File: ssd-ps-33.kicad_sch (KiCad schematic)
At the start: 0 parts

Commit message: Put controller and filter capacitors to schematic
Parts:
- added C1, C2: 10uF, Capacitor_SMD:C_0805_2012Metric, symbol Device:C
- added C3: 0.1uF, Capacitor_SMD:C_0603_1608Metric_Pad1.08x0.95mm_HandSolder, symbol Device:C
- added C4, C5, C6: 22uF, Capacitor_SMD:C_0805_2012Metric, symbol Device:C
- added L1: 2.2µH, symbol Device:L_Ferrite
- added U1: TPS563252, Package_TO_SOT_SMD:SOT-563, symbol ssd-ps-33:TPS56325x
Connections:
- new net GND: U1.3 (GND)

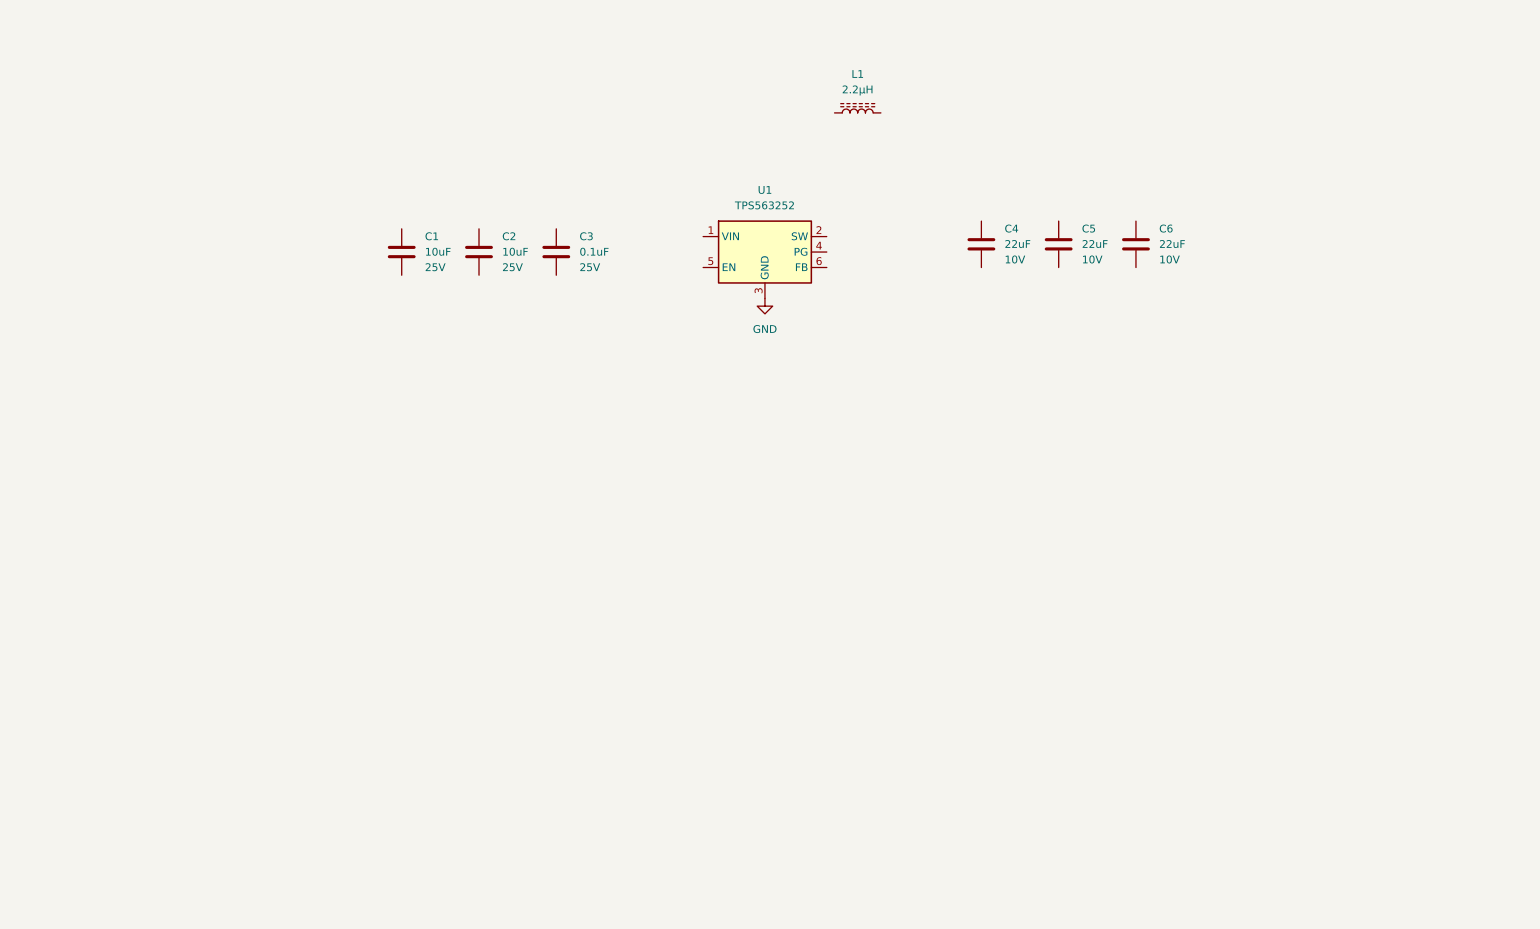
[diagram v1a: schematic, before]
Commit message: Create main schematics without connectors for now
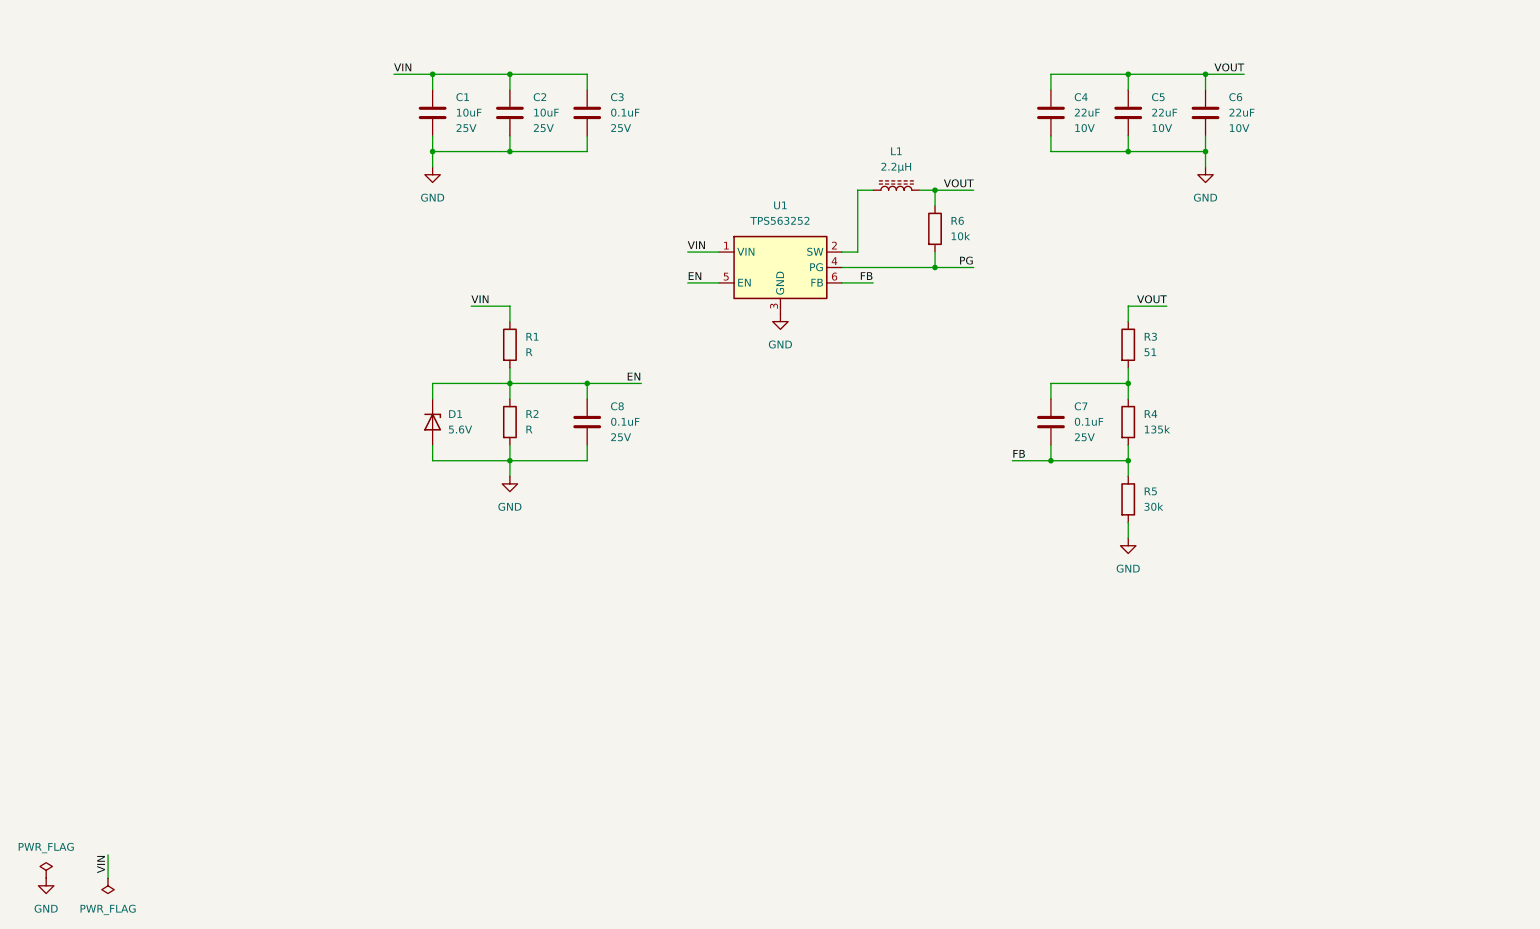
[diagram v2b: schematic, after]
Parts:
- added C7, C8: 0.1uF, Capacitor_SMD:C_0603_1608Metric_Pad1.08x0.95mm_HandSolder, symbol Device:C
- added D1: 5.6V, Diode_SMD:D_SOD-323_HandSoldering, symbol Device:D_Zener
- added R1, R2: R, Resistor_SMD:R_0603_1608Metric_Pad0.98x0.95mm_HandSolder, symbol Device:R
- added R3: 51, Resistor_SMD:R_0603_1608Metric_Pad0.98x0.95mm_HandSolder, symbol Device:R
- added R4: 135k, Resistor_SMD:R_0603_1608Metric_Pad0.98x0.95mm_HandSolder, symbol Device:R
- added R5: 30k, Resistor_SMD:R_0603_1608Metric_Pad0.98x0.95mm_HandSolder, symbol Device:R
- added R6: 10k, Resistor_SMD:R_0603_1608Metric_Pad0.98x0.95mm_HandSolder, symbol Device:R
- L1: footprint (none) -> Inductor_SMD:L_Chilisin_BWVS00505040
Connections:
- net GND: now also C1.2, C2.2, C3.2, C4.2, C5.2, C6.2, C8.2, D1.2 (A), R2.2, R5.2
- net VOUT: now reaches C4.1
- net VOUT: now also C5.1, C6.1, L1.2, R3.1, R6.1
- net at L1.1: now also U1.2 (SW)
- net VIN: now reaches U1.1 (VIN)
- net VIN: now also C1.1, C2.1, C3.1, R1.1
- net PG: now reaches U1.4 (PG)
- net PG: now also R6.2
- net EN: now reaches U1.5 (EN)
- net EN: now also C8.1, D1.1 (K), R1.2, R2.1
- net FB: now reaches U1.6 (FB)
- net FB: now also C7.2, R4.2, R5.1
- new net: C7.1, R3.2, R4.1
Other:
- moved on the sheet: C1, C2, C3, C4, C5, C6, L1, U1

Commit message: Draft routing, board size and select connectors
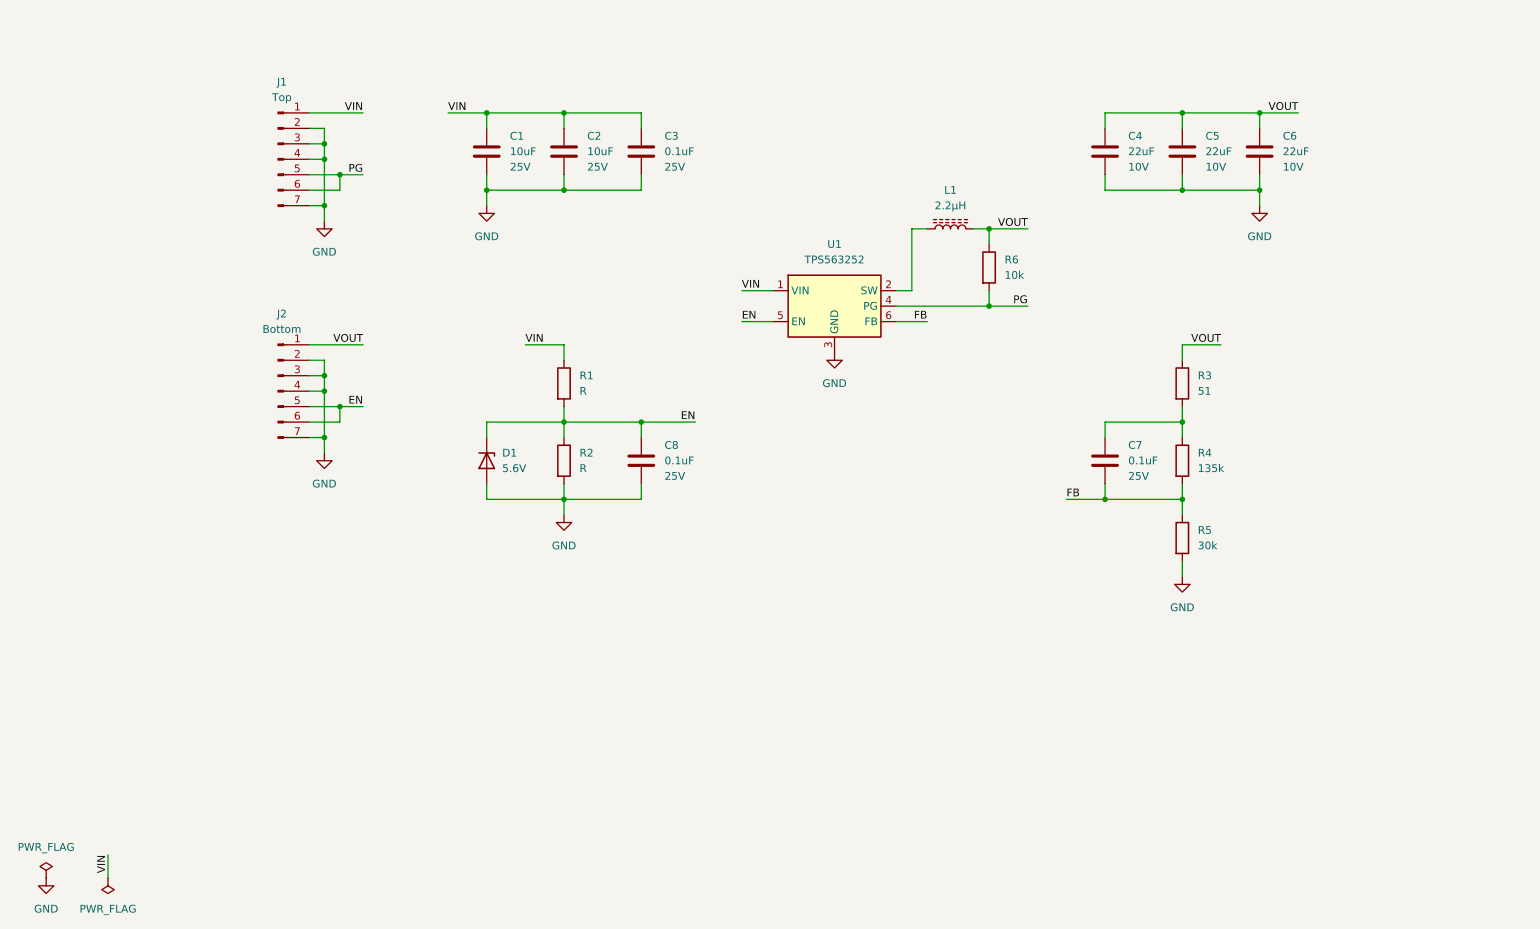
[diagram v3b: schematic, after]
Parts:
- added J1: Top, ssd-ps-33:PinHeader_1x07_P2.54mm_Vertical_No_Silkscreen, symbol Connector:Conn_01x07_Pin
- added J2: Bottom, ssd-ps-33:PinHeader_1x07_P2.54mm_Vertical_No_Silkscreen, symbol Connector:Conn_01x07_Pin
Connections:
- net EN: now also J2.5 (Pin_5), J2.6 (Pin_6)
- net GND: now also J1.2 (Pin_2), J1.3 (Pin_3), J1.4 (Pin_4), J1.7 (Pin_7), J2.2 (Pin_2), J2.3 (Pin_3), J2.4 (Pin_4), J2.7 (Pin_7)
- net PG: now also J1.5 (Pin_5), J1.6 (Pin_6)
- net VIN: now also J1.1 (Pin_1)
- net VOUT: now also J2.1 (Pin_1)
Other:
- moved on the sheet: C1, C2, C3, C4, C5, C6, C7, C8, D1, L1, R1, R2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

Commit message: Set values for enable network and fix DRC errors
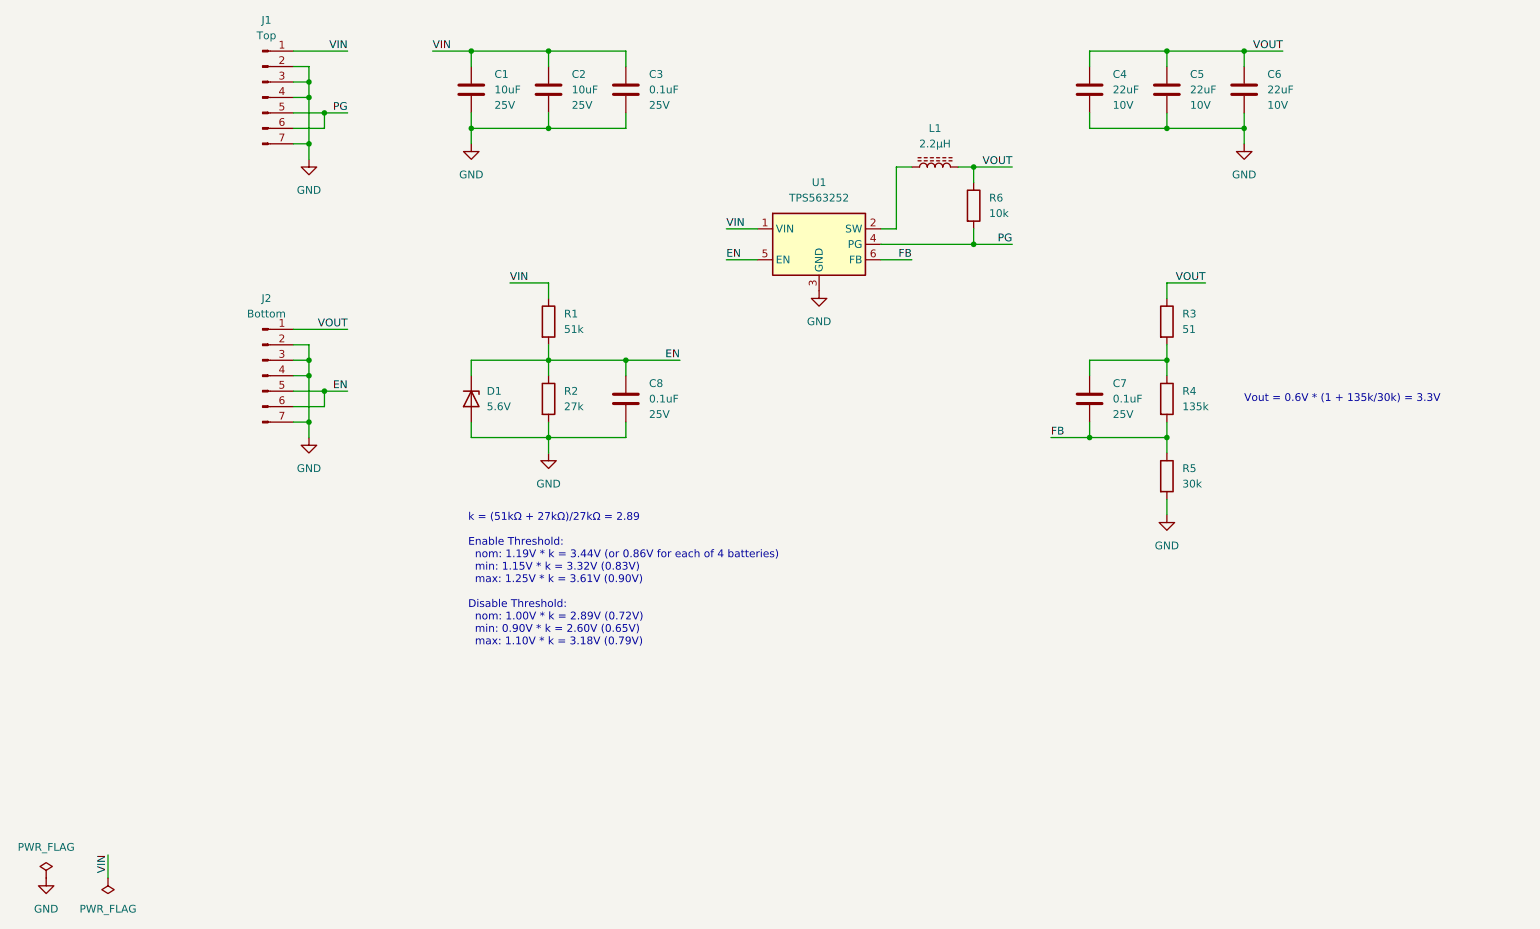
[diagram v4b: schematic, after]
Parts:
- R1: value R -> 51k
- R2: value R -> 27k
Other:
- note added: "Vout = 0.6V * (1 + 135k/30k) = 3.3V"
- note added: "k = (51kΩ + 27kΩ)/27kΩ = 2.89 Enable Threshold: nom: 1.19V * k = 3.44V (or 0.86V for each of 4 batteries) min: 1.15V * k = 3.32V (0.83V) max: 1.25V * k = 3.61V (0.90V) Disable Threshold: nom: 1.00V * k = 2.89V (0.72V) min: 0.90V * k = 2.60V (0.65V) max: 1.10V * k = 3.18V (0.79V)"
- moved on the sheet: C1, C2, C3, C4, C5, C6, C7, C8, D1, J1, J2, L1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

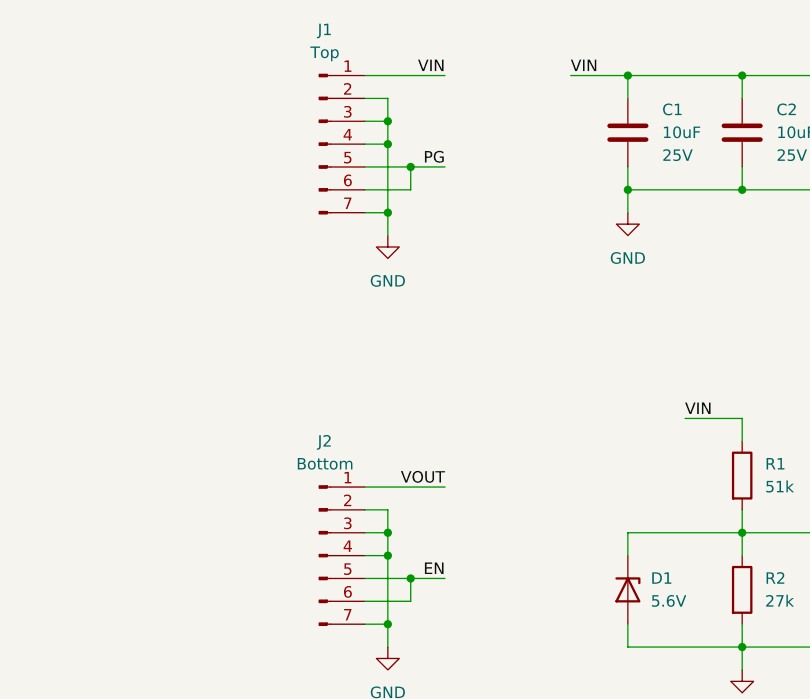
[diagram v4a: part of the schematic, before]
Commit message: Add designators to pins and board name
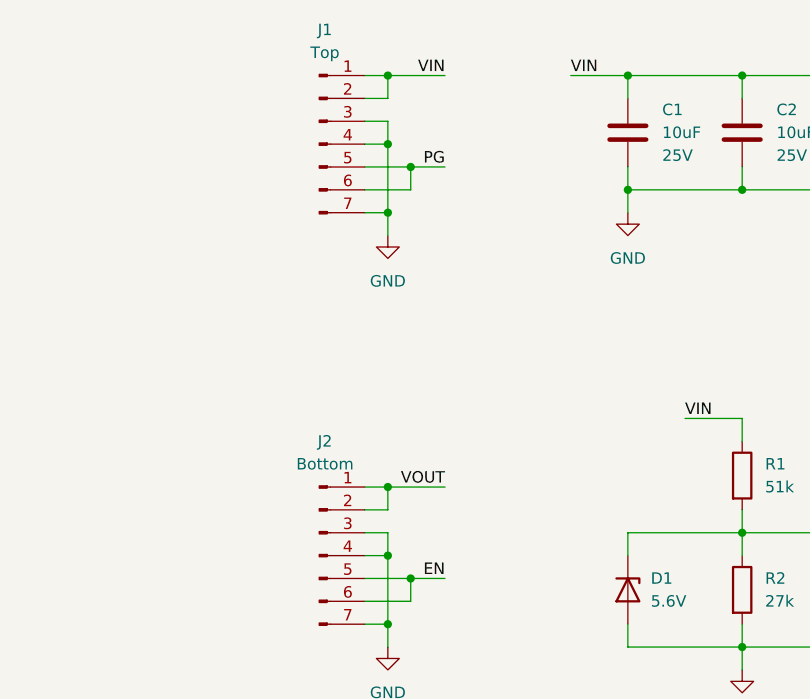
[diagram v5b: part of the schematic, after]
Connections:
- net GND: no longer J1.2 (Pin_2), J2.2 (Pin_2)
- net VIN: now also J1.2 (Pin_2)
- net VOUT: now also J2.2 (Pin_2)
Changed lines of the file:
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@@
+	)
+	(junction
+		(at 62.23 59.69)
+		(diameter 0)
+		(color 0 0 0 0)
 	)
 	(junction
@@
 	)
 	(junction
-		(at 62.23 110.49)
-		(diameter 0)
-		(color 0 0 0 0)
-	)
-	(junction
 		(at 203.2 59.69)
 		(diameter 0)
@@
 	)
 	(junction
-		(at 62.23 64.77)
+		(at 62.23 105.41)
 		(diameter 0)
 		(color 0 0 0 0)
@@
 	(wire
 		(pts
-			(xy 62.23 64.77) (xy 62.23 62.23)
-		)
-		(stroke
-			(width 0)
-			(type default)
-		)
-	)
-	(wire
-		(pts
 			(xy 158.75 88.9) (xy 156.21 88.9)
 		)
@@
 	(wire
 		(pts
-			(xy 62.23 107.95) (xy 62.23 110.49)
-		)
-		(stroke
-			(width 0)
-			(type default)
-		)
-	)
-	(wire
-		(pts
 			(xy 114.3 110.49) (xy 114.3 113.03)
 		)
@@
 	(wire
 		(pts
+			(xy 62.23 59.69) (xy 62.23 62.23)
+		)
+		(stroke
+			(width 0)
+			(type default)
+		)
+	)
+	(wire
+		(pts
 			(xy 190.5 62.23) (xy 190.5 59.69)
 		)
@@
 	(wire
 		(pts
+			(xy 62.23 105.41) (xy 62.23 107.95)
+		)
+		(stroke
+			(width 0)
+			(type default)
+		)
+	)
+	(wire
+		(pts
 			(xy 184.15 123.19) (xy 190.5 123.19)
 		)
@@
 	(wire
 		(pts
-			(xy 68.58 105.41) (xy 59.69 105.41)
+			(xy 68.58 105.41) (xy 62.23 105.41)
 		)
 		(stroke
@@
 	(wire
 		(pts
+			(xy 62.23 59.69) (xy 59.69 59.69)
+		)
+		(stroke
+			(width 0)
+			(type default)
+		)
+	)
+	(wire
+		(pts
 			(xy 171.45 78.74) (xy 171.45 81.28)
 		)
@@
 	(wire
 		(pts
+			(xy 62.23 105.41) (xy 59.69 105.41)
+		)
+		(stroke
+			(width 0)
+			(type default)
+		)
+	)
+	(wire
+		(pts
 			(xy 130.81 88.9) (xy 135.89 88.9)
 		)
@@
 	(wire
 		(pts
-			(xy 68.58 59.69) (xy 59.69 59.69)
-		)
-		(stroke
+			(xy 68.58 59.69) (xy 62.23 59.69)
+		)
+		(stroke

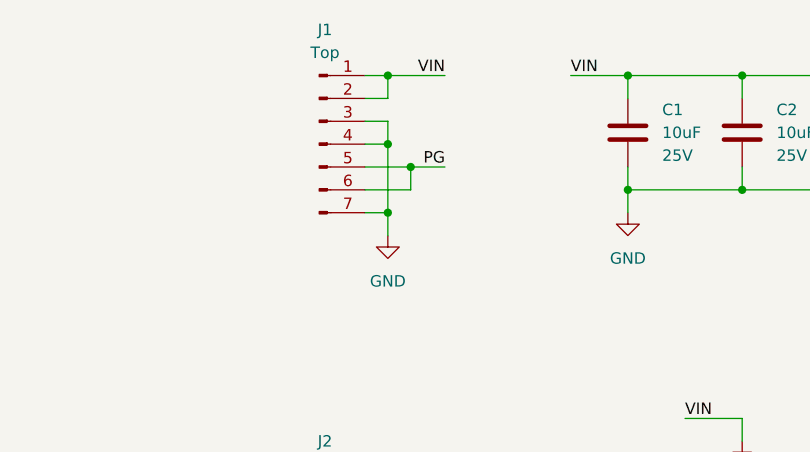
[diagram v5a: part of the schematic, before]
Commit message: Add FB to top connector and finalize routing
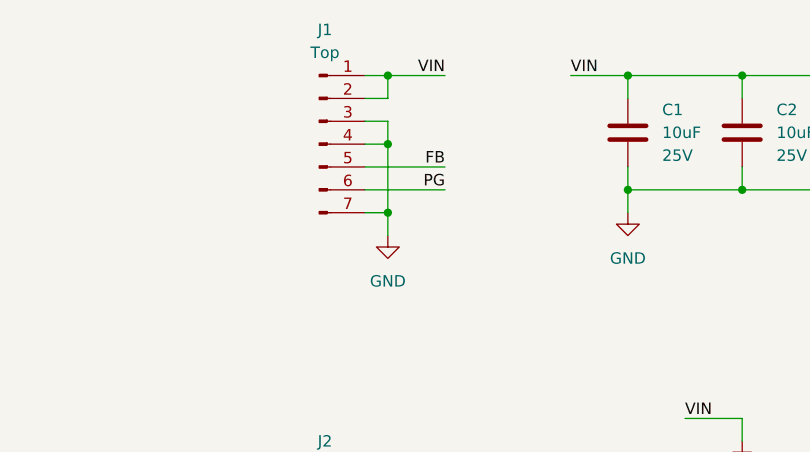
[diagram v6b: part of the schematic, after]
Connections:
- net FB: now also J1.5 (Pin_5)
- net PG: no longer J1.5 (Pin_5)
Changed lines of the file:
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@@
-	)
-	(junction
-		(at 64.77 69.85)
-		(diameter 0)
-		(color 0 0 0 0)
 	)
 	(junction
@@
 	(wire
 		(pts
-			(xy 59.69 69.85) (xy 64.77 69.85)
-		)
-		(stroke
-			(width 0)
-			(type default)
-		)
-	)
-	(wire
-		(pts
 			(xy 190.5 72.39) (xy 203.2 72.39)
 		)
@@
 	(wire
 		(pts
-			(xy 59.69 72.39) (xy 64.77 72.39)
+			(xy 59.69 72.39) (xy 68.58 72.39)
 		)
 		(stroke
@@
 	(wire
 		(pts
-			(xy 68.58 69.85) (xy 64.77 69.85)
-		)
-		(stroke
-			(width 0)
-			(type default)
-		)
-	)
-	(wire
-		(pts
 			(xy 88.9 72.39) (xy 101.6 72.39)
 		)
@@
 	(wire
 		(pts
-			(xy 64.77 72.39) (xy 64.77 69.85)
-		)
-		(stroke
-			(width 0)
-			(type default)
-		)
-	)
-	(wire
-		(pts
 			(xy 114.3 110.49) (xy 123.19 110.49)
+		)
+		(stroke
+			(width 0)
+			(type default)
+		)
+	)
+	(wire
+		(pts
+			(xy 59.69 69.85) (xy 68.58 69.85)
 		)
 		(stroke
@@
 		)
 	)
+	(label "FB"
+		(at 68.58 69.85 180)
+		(effects
+			(font
+				(size 1.27 1.27)
+			)
+			(justify right bottom)
+		)
+	)
 	(label "EN"
 		(at 68.58 115.57 180)
@@
 	)
 	(label "PG"
-		(at 68.58 69.85 180)
-		(effects
-			(font
+		(at 68.58 72.39 180)
+		(effects
+			(font
